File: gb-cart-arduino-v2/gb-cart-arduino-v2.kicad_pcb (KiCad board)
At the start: 2 copper layers, 57.5 x 53.5 mm, 18 parts, among them J1 Conn_01x16_Pin, U1 74HC595, U2 74HC595

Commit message: Rewired v2
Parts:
- removed Ce1: 10uF, Capacitor_SMD:C_1206_3216Metric
- removed Ra1, Ra2, Ra4: 470, Resistor_SMD:R_1206_3216Metric
- removed Rd8: 1k, Resistor_SMD:R_1206_3216Metric
- added C1: 10uF, Capacitor_SMD:C_1206_3216Metric, F.Cu at (150.5, 96.0)
- added Rd0: 1k, Resistor_SMD:R_1206_3216Metric, F.Cu at (114.5, 108.5)
- added Rl1: 470, Resistor_SMD:R_1206_3216Metric, F.Cu at (150.5, 108.0)
- added Rr1: 470, Resistor_SMD:R_1206_3216Metric, F.Cu at (150.5, 104.0)
- added Rw1: 470, Resistor_SMD:R_1206_3216Metric, F.Cu at (150.5, 100.0)
- moved Rd4 12.1 mm to (109.5, 96.5), turned to 0 degrees
- moved Rd5 11.3 mm to (109.5, 100.5)
- moved Rd3 11.1 mm to (114.5, 96.5)
- moved Rd7 9.97 mm to (109.5, 108.5)
- moved Rd1 8.23 mm to (114.5, 104.5)
- moved Rd6 8.06 mm to (109.5, 104.5)
- moved Rd2 6.84 mm to (114.5, 100.5)
- moved D1 6.50 mm to (150.6, 112.0), turned to 0 degrees
- moved Rreset1 5.63 mm to (102.5, 97.5), turned to 90 degrees
- moved J1 3.53 mm to (144.8, 119.5)
- moved U1 3.20 mm to (140.0, 101.5)
- moved U2 2.50 mm to (126.5, 101.5)
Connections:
- D1 pad 2: /VCC -> /LED
- J1 pad 7: /Address_Clock -> /Address_Latch
- J1 pad 8: /Address_Latch -> /Address_Clock
- Rd1 pad 1: /Data_7 -> /Data_1
- Rd2 pad 1: /Data_6 -> /Data_2
- Rd3 pad 1: /Data_5 -> /Data_3
- Rd5 pad 1: /Data_3 -> /Data_5
- Rd6 pad 1: /Data_2 -> /Data_6
- Rd7 pad 1: /Data_1 -> /Data_7
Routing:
- net /VCC: track 95.8 -> 130.5 mm, vias 8 -> 5
- net /GND: track 199.4 -> 173.0 mm, vias 7 -> 5
- net /Address_Clock: track 27.2 -> 43.4 mm, vias 2 -> 0
- net /Address_Latch: track 33.3 -> 43.7 mm, vias 2 -> 0
- net /Write: track 28.0 -> 37.6 mm
- net /Data_3: track 29.4 -> 35.2 mm
- net /Address_7: track 23.7 -> 18.2 mm
- net /Clock: track 41.7 -> 36.3 mm
- net /Address_0: track 15.2 -> 10.0 mm
- net /Address_6: track 21.4 -> 16.3 mm
- net /Address_5: track 19.4 -> 14.4 mm
- net /Data_2: track 30.8 -> 35.3 mm
- net /Serial_Chain: track 28.7 -> 24.4 mm
- net /Address_15: track 21.8 -> 17.5 mm
- net /LED: track 0.00 -> 4.02 mm
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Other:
- board size 57.5 x 53.5 mm -> 57.5 x 55 mm

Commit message: Update
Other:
- board size 57.5 x 55 mm -> 58.5 x 56.2 mm
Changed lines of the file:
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@@
 		(tags "resistor")
 		(property "Reference" "Rl1"
-			(at 0 -1.83 0)
+			(at 0 2 0)
 			(layer "F.SilkS")
 			(effects
@@
 		(tags "LED")
 		(property "Reference" "D1"
-			(at 0 -1.83 0)
+			(at -0.1 -2 0)
 			(layer "F.SilkS")
 			(effects
@@
 		)
 	)
-	(gr_rect
-		(start 97 66.5)
-		(end 154.5 121.5)
+	(gr_line
+		(start 97.5 66)
+		(end 154 66)
+		(stroke
+			(width 0.1)
+			(type default)
+		)
+		(layer "Edge.Cuts")
+	)
+	(gr_line
+		(start 96.5 121.175)
+		(end 96.5 67)
+		(stroke
+			(width 0.1)
+			(type default)
+		)
+		(layer "Edge.Cuts")
+	)
+	(gr_line
+		(start 154 122.175)
+		(end 97.5 122.175)
+		(stroke
+			(width 0.1)
+			(type default)
+		)
+		(layer "Edge.Cuts")
+	)
+	(gr_arc
+		(start 155 121.175)
+		(mid 154.707107 121.882107)
+		(end 154 122.175)
+		(stroke
+			(width 0.1)
+			(type default)
+		)
+		(layer "Edge.Cuts")
+	)
+	(gr_arc
+		(start 97.5 122.175)
+		(mid 96.792893 121.882107)
+		(end 96.5 121.175)
+		(stroke
+			(width 0.1)
+			(type default)
+		)
+		(layer "Edge.Cuts")
+	)
+	(gr_line
+		(start 155 67)
+		(end 155 121.175)
+		(stroke
+			(width 0.1)
+			(type default)
+		)
+		(layer "Edge.Cuts")
+	)
+	(gr_arc
+		(start 154 66)
+		(mid 154.707107 66.292893)
+		(end 155 67)
+		(stroke
+			(width 0.1)
+			(type default)
+		)
+		(layer "Edge.Cuts")
+	)
+	(gr_arc
+		(start 96.5 67)
+		(mid 96.792893 66.292893)
+		(end 97.5 66)
 		(stroke
 			(width 0.1)
 			(type default)
 		)
-		(fill no)
 		(layer "Edge.Cuts")
 	)
@@
 	)
 	(segment
-		(start 118.0385 95.001)
-		(end 118.0375 95)
-		(width 0.3)
-		(layer "F.Cu")
-		(net 7)
-	)
-	(segment
 		(start 116.314979 117.0235)
 		(end 115.0865 115.795021)
@@
 	)
 	(segment
-		(start 121.4775 116.5225)
-		(end 121.455 116.5)
-		(width 0.3)
-		(layer "F.Cu")
-		(net 10)
-	)
-	(segment
 		(start 115.5875 108.9125)
 		(end 116 108.5)
@@
 		(width 0.3)
 		(layer "F.Cu")
-		(net 22)
-	)
-	(segment
-		(start 133.501 95.001)
-		(end 133.502 95)
-		(width 0.3)
-		(layer "F.Cu")

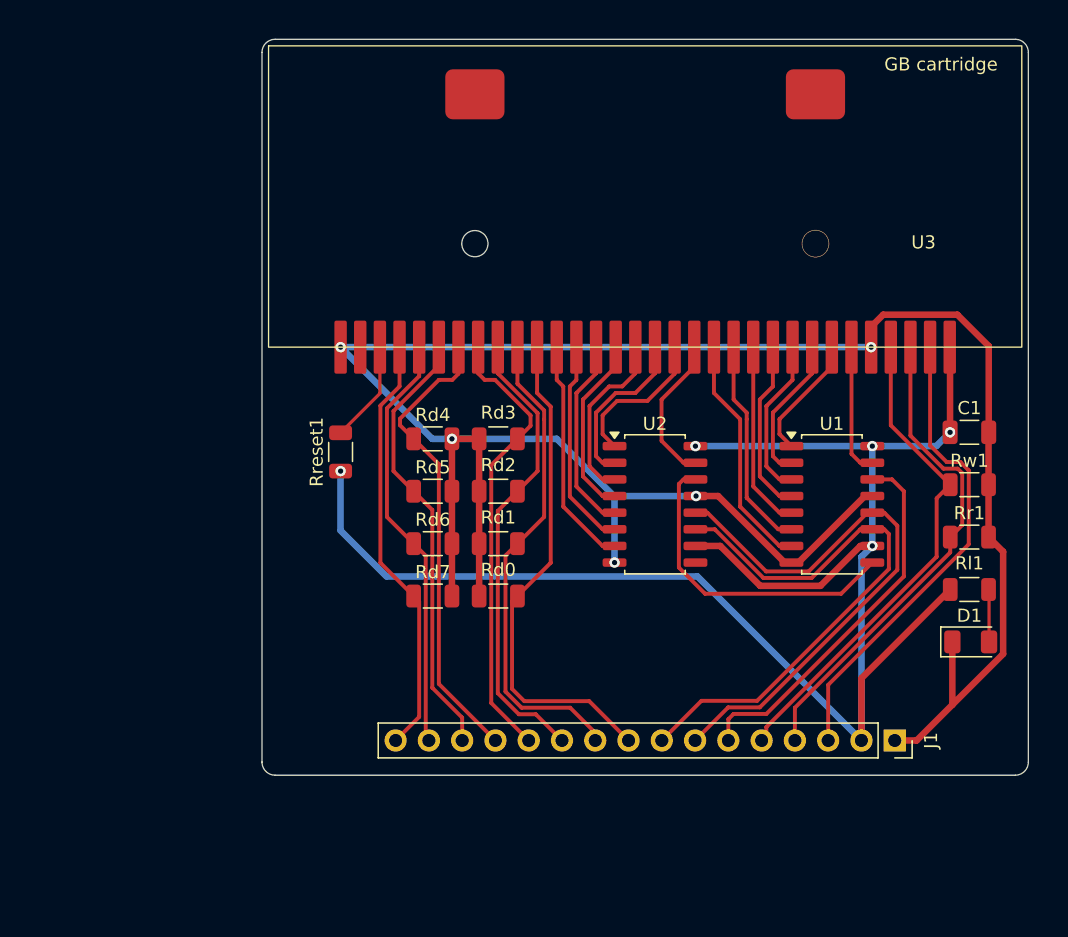
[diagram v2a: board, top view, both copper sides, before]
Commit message: Added texts
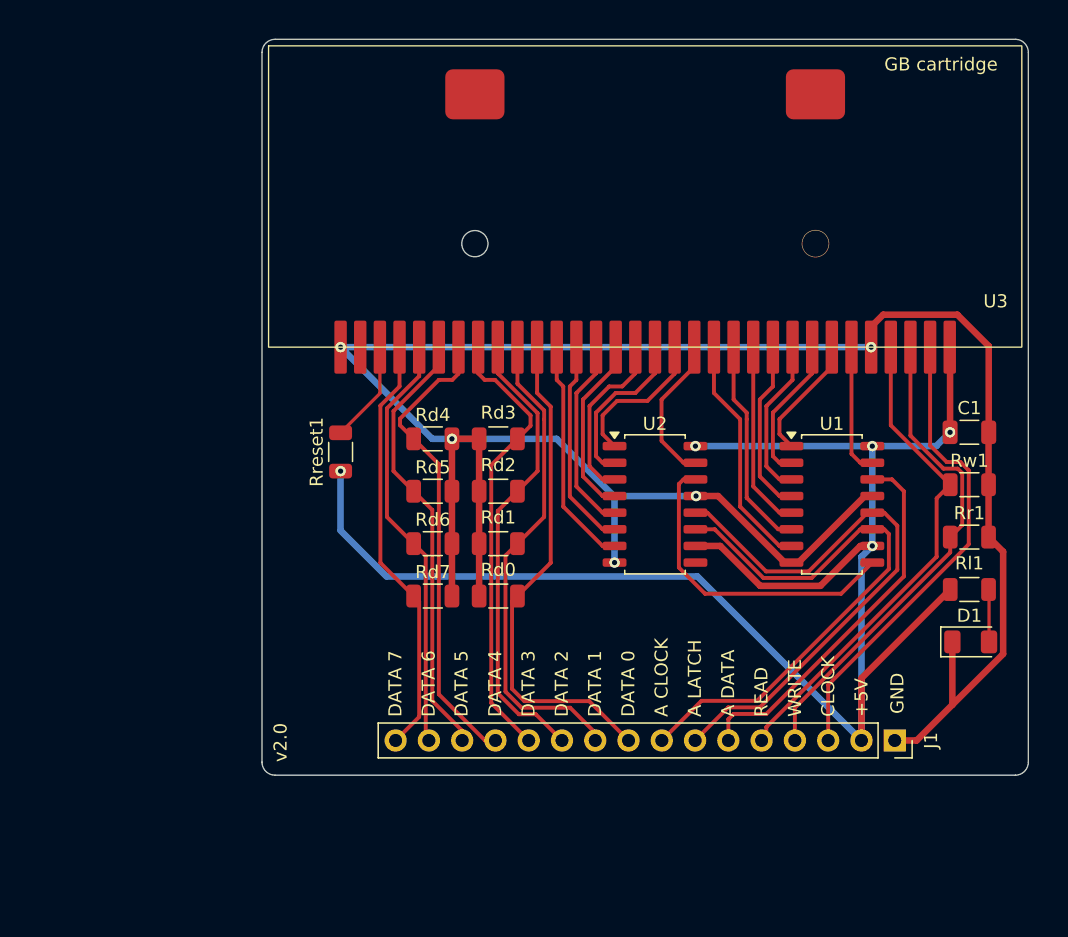
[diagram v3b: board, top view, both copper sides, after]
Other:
- board text added: "+5V"
- board text added: "A CLOCK"
- board text added: "A DATA"
- board text added: "A LATCH"
- board text added: "CLOCK"
- board text added: "DATA 0"
- board text added: "DATA 1"
- board text added: "DATA 2"
- board text added: "DATA 3"
- board text added: "DATA 4"
- board text added: "DATA 5"
- board text added: "DATA 6"
- board text added: "DATA 7"
- board text added: "GND"
- board text added: "READ"
- board text added: "WRITE"
- board text added: "https://github.com/GreenOlvi/gb-cart-reader-schematics"
- board text added: "v2.0"
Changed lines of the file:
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@@
 		(at 149 89.5)
 		(property "Reference" "U3"
-			(at -2 -8 0)
+			(at 3.5 -3.5 0)
 			(unlocked yes)
 			(layer "F.SilkS")
@@
 		(layer "Edge.Cuts")
 	)
+	(gr_text "CLOCK"
+		(at 139.72 117.725 90)
+		(layer "F.SilkS")
+		(effects
+			(font
+				(size 1 1)
+				(thickness 0.15)
+			)
+			(justify left)
+		)
+	)
+	(gr_text "A DATA"
+		(at 132.08 117.729 90)
+		(layer "F.SilkS")
+		(effects
+			(font
+				(size 1 1)
+				(thickness 0.15)
+			)
+			(justify left)
+		)
+	)
+	(gr_text "DATA 3"
+		(at 116.84 117.729 90)
+		(layer "F.SilkS")
+		(effects
+			(font
+				(size 1 1)
+				(thickness 0.15)
+			)
+			(justify left)
+		)
+	)
+	(gr_text "DATA 7"
+		(at 106.68 117.729 90)
+		(layer "F.SilkS")
+		(effects
+			(font
+				(size 1 1)
+				(thickness 0.15)
+			)
+			(justify left)
+		)
+	)
+	(gr_text "DATA 6"
+		(at 109.22 117.729 90)
+		(layer "F.SilkS")
+		(effects
+			(font
+				(size 1 1)
+				(thickness 0.15)
+			)
+			(justify left)
+		)
+	)
+	(gr_text "v2.0"
+		(at 98.5 121.175 90)
+		(layer "F.SilkS")
+		(effects
+			(font
+				(size 1 1)
+				(thickness 0.15)
+			)
+			(justify left bottom)
+		)
+	)
+	(gr_text "A CLOCK"
+		(at 127 117.729 90)
+		(layer "F.SilkS")
+		(effects
+			(font
+				(size 1 1)
+				(thickness 0.15)
+			)
+			(justify left)
+		)
+	)
+	(gr_text "GND"
+		(at 145 117.5 90)
+		(layer "F.SilkS")
+		(effects
+			(font
+				(size 1 1)
+				(thickness 0.15)
+			)
+			(justify left)
+		)
+	)
+	(gr_text "DATA 5"
+		(at 111.725 117.725 90)
+		(layer "F.SilkS")
+		(effects
+			(font
+				(size 1 1)
+				(thickness 0.15)
+			)
+			(justify left)
+		)
+	)
+	(gr_text "DATA 2"
+		(at 119.38 117.729 90)
+		(layer "F.SilkS")
+		(effects
+			(font
+				(size 1 1)
+				(thickness 0.15)
+			)
+			(justify left)
+		)
+	)
+	(gr_text "DATA 4"
+		(at 114.3 117.729 90)
+		(layer "F.SilkS")
+		(effects
+			(font
+				(size 1 1)
+				(thickness 0.15)
+			)
+			(justify left)
+		)
+	)
+	(gr_text "READ"
+		(at 134.62 117.725 90)
+		(layer "F.SilkS")
+		(effects
+			(font
+				(size 1 1)
+				(thickness 0.15)
+			)
+			(justify left)
+		)
+	)
+	(gr_text "DATA 0"
+		(at 124.46 117.725 90)
+		(layer "F.SilkS")
+		(effects
+			(font
+				(size 1 1)
+				(thickness 0.15)
+			)
+			(justify left)
+		)
+	)
+	(gr_text "WRITE"
+		(at 137.18 117.725 90)
+		(layer "F.SilkS")
+		(effects
+			(font
+				(size 1 1)
+				(thickness 0.15)
+			)
+			(justify left)
+		)
+	)
+	(gr_text "DATA 1"
+		(at 121.92 117.729 90)
+		(layer "F.SilkS")
+		(effects
+			(font
+				(size 1 1)
+				(thickness 0.15)
+			)
+			(justify left)
+		)
+	)
+	(gr_text "A LATCH"
+		(at 129.54 117.729 90)
+		(layer "F.SilkS")
+		(effects
+			(font
+				(size 1 1)
+				(thickness 0.15)
+			)
+			(justify left)
+		)
+	)
+	(gr_text "+5V"
+		(at 142.26 117.725 90)
+		(layer "F.SilkS")
+		(effects
+			(font
+				(size 1 1)
+				(thickness 0.15)
+			)
+			(justify left)
+		)
+	)
+	(gr_text "https://github.com/GreenOlvi/gb-cart-reader-schematics"
+		(at 154 68.5 0)
+		(layer "B.SilkS")
+		(effects
+			(font
+				(size 1.1 1.1)
+				(thickness 0.22)
+				(bold yes)
+			)
+			(justify left bottom mirror)
+		)
+	)
 	(segment
 		(start 113.075 108.5)
@@
 	)
 	(segment
-		(start 109.5 101.925)
-		(end 108.075 100.5)
+		(start 111.78 119.525)
+		(end 111.78 118.78)
 		(width 0.3)
 		(layer "F.Cu")
@@
 	)
 	(segment
-		(start 111.78 117.78)
-		(end 109.5 115.5)
+		(start 108.075 100.5)
+		(end 106.5375 98.9625)
 		(width 0.3)
 		(layer "F.Cu")
@@
 	)
 	(segment
-		(start 108.075 100.5)
-		(end 106.5375 98.9625)
+		(start 111.78 118.78)
+		(end 109.5 116.5)
 		(width 0.3)
 		(layer "F.Cu")
@@
 	)
 	(segment
-		(start 111.78 119.525)
-		(end 111.78 117.78)
+		(start 109.5 116.5)
+		(end 109.5 101.925)
 		(width 0.3)
 		(layer "F.Cu")
@@
 	)
 	(segment
-		(start 109.5 115.5)
-		(end 109.5 101.925)
+		(start 109.5 101.925)
+		(end 108.075 100.5)
 		(width 0.3)
 		(layer "F.Cu")
@@
 	)
 	(segment
-		(start 107.0385 95.4635)
+		(start 110 98.425)
 		(end 108.075 96.5)
 		(width 0.3)
@@
 	)
 	(segment
-		(start 110 98.425)
-		(end 108.075 96.5)
+		(start 113.525 119.525)
+		(end 110 116)
 		(width 0.3)
 		(layer "F.Cu")
@@
 	)
 	(segment
-		(start 110 115.205)
-		(end 110 98.425)
+		(start 107.0385 95.4635)
+		(end 108.075 96.5)
 		(width 0.3)
 		(layer "F.Cu")
@@
 	)
 	(segment
+		(start 111.5 91.525)
+		(end 111.025 92)
+		(width 0.3)
+		(layer "F.Cu")
+		(net 15)
+	)
+	(segment
 		(start 114.32 119.525)
-		(end 110 115.205)
+		(end 113.525 119.525)
 		(width 0.3)
 		(layer "F.Cu")
@@
 	)
 	(segment
-		(start 111.5 91.525)
-		(end 111.025 92)
+		(start 110 116)
+		(end 110 98.425)
 		(width 0.3)
 		(layer "F.Cu")

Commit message: Final sent to production
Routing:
- net /GND: track 173.0 -> 176.2 mm, vias 5 -> 4
- added copper zone on B.Cu, net /GND
- added copper zone on F.Cu, net /GND
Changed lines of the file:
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@@
 			(outputformat 1)
 			(mirror no)
-			(drillshape 1)
+			(drillshape 0)
 			(scaleselection 1)
-			(outputdirectory "")
+			(outputdirectory "gerber/")
 		)
 	)
@@
 		)
 	)
-	(gr_text "v2.0"
-		(at 98.5 121.175 90)
-		(layer "F.SilkS")
-		(effects
-			(font
-				(size 1 1)
-				(thickness 0.15)
-			)
-			(justify left bottom)
-		)
-	)
 	(gr_text "A CLOCK"
 		(at 127 117.729 90)
@@
 		)
 	)
+	(gr_text "v2.0"
+		(at 154 70.5 0)
+		(layer "B.SilkS")
+		(effects
+			(font
+				(size 1 1)
+				(thickness 0.15)
+			)
+			(justify left bottom mirror)
+		)
+	)
 	(gr_text "https://github.com/GreenOlvi/gb-cart-reader-schematics"
 		(at 154 68.5 0)
@@
 	)
 	(segment
+		(start 102.5 87.475)
+		(end 102.5 89.5)
+		(width 0.5)
+		(layer "F.Cu")
+		(net 2)
+	)
+	(segment
 		(start 111 104.5)
 		(end 111 108.5)
@@
 	)
 	(segment
+		(start 144 87.024)
+		(end 143.917714 87.024)
+		(width 0.5)
+		(layer "F.Cu")
+		(net 2)
+	)
+	(segment
 		(start 143.917714 87.024)
 		(end 143 87.941714)
@@
 	(segment
 		(start 149.582286 87.024)
-		(end 143.917714 87.024)
+		(end 144 87.024)
 		(width 0.5)
 		(layer "F.Cu")
@@
 	)
 	(segment
+		(start 102.951 87.024)
+		(end 102.5 87.475)
+		(width 0.5)
+		(layer "F.Cu")
+		(net 2)
+	)
+	(segment
 		(start 151.9625 104)
 		(end 151.9625 96.0125)
@@
 	)
 	(segment
+		(start 144 87.024)
+		(end 102.951 87.024)
+		(width 0.5)
+		(layer "F.Cu")
+		(net 2)
+	)
+	(segment
 		(start 129.635 100.865)
 		(end 131.319878 100.865)
@@
 	)
 	(via
-		(at 143 89.5)
-		(size 0.8)
-		(drill 0.4)
-		(layers "F.Cu" "B.Cu")
-		(net 2)
-	)
-	(via
 		(at 102.5 89.5)
 		(size 0.8)
@@
 	)
 	(segment
-		(start 143 89.5)
-		(end 102.5 89.5)
-		(width 0.5)
-		(layer "B.Cu")
-		(net 2)
-	)
-	(segment
 		(start 123.4125 101.0875)
 		(end 123.4125 105.945)
@@
 		(net 37)
 	)
+	(zone
+		(net 2)
+		(net_name "/GND")
+		(layers "F.Cu" "B.Cu")
+		(hatch edge 0.5)
+		(connect_pads
+			(clearance 0.5)
+		)
+		(min_thickness 0.25)
+		(filled_areas_thickness no)
+		(fill yes
+			(thermal_gap 0.5)
+			(thermal_bridge_width 0.5)
+		)
+		(polygon
+			(pts
+				(xy 95 65) (xy 156 65) (xy 156 123.5) (xy 95 123.5)
+			)
+		)
+	)
 	(embedded_fonts no)

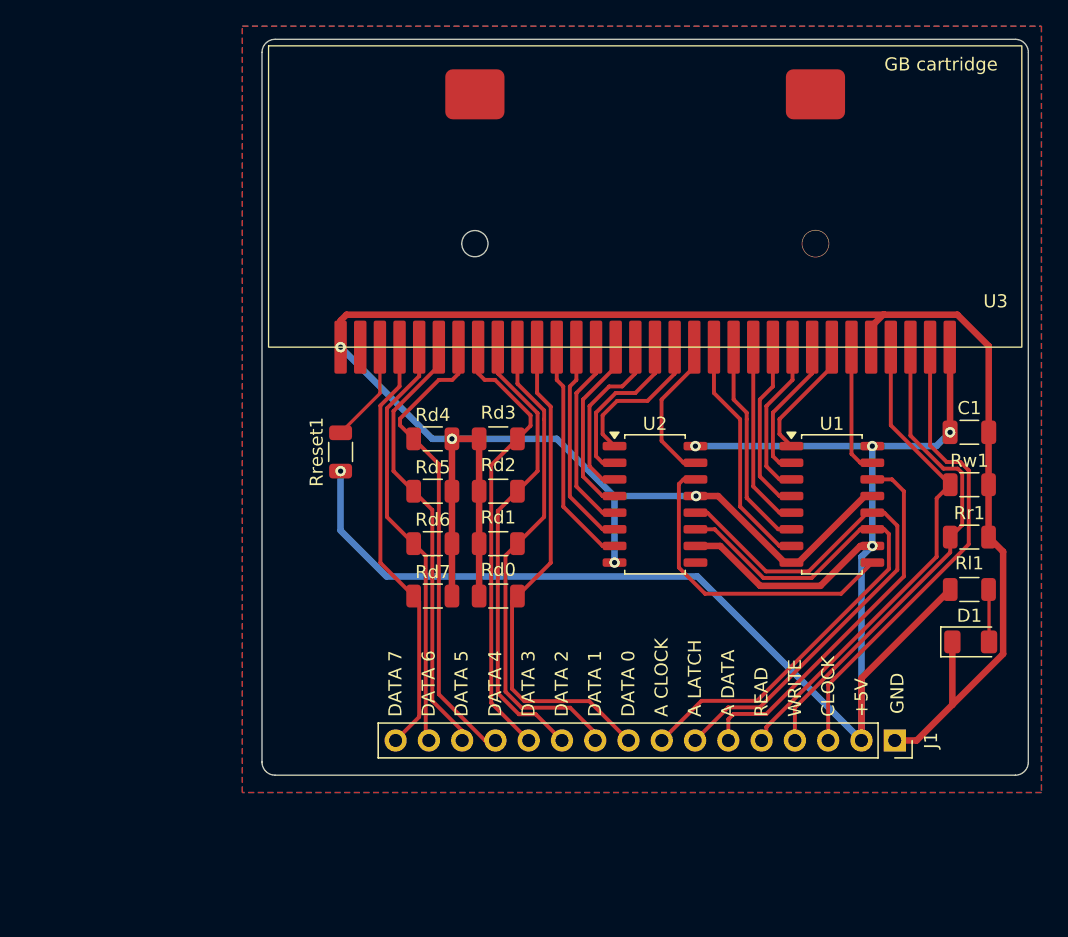
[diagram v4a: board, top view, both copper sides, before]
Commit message: Reversed gb cart connector footprint
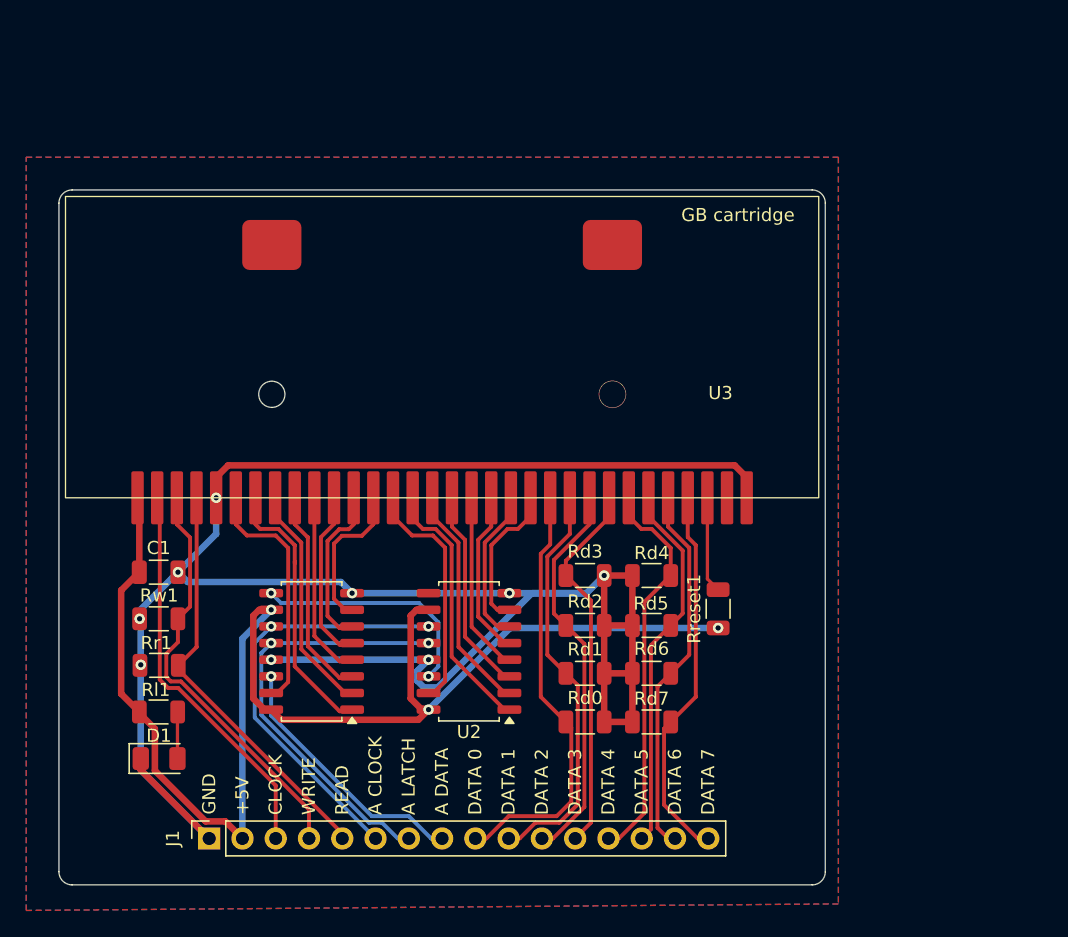
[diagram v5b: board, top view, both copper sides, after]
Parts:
- moved C1 62.8 mm to (88.6, 106.7)
- moved Rw1 62.7 mm to (88.6, 110.2), turned to 180 degrees
- moved Rr1 62.6 mm to (88.6, 113.8), turned to 180 degrees
- moved Rl1 62.6 mm to (88.6, 117.3)
- moved D1 62.6 mm to (88.6, 120.9)
- moved J1 52.9 mm to (92.5, 127.0), turned to 90 degrees
- moved U1 41.3 mm to (100.3, 112.7), turned to 180 degrees
- moved Rreset1 31.2 mm to (131.3, 109.5)
- moved Rd4 19.7 mm to (126.2, 106.9), turned to 180 degrees
- moved Rd5 19.6 mm to (126.2, 110.7), turned to 180 degrees
- moved Rd6 19.4 mm to (126.2, 114.4), turned to 180 degrees
- moved U3 19.3 mm to (133.5, 101.0)
- moved Rd7 19.3 mm to (126.2, 118.1), turned to 180 degrees
- moved U2 18.1 mm to (112.3, 112.7), turned to 180 degrees
- moved Rd3 12.4 mm to (121.2, 106.9), turned to 0 degrees
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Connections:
- J1 pad 6: /Address_Data -> /Address_Clock
- J1 pad 8: /Address_Clock -> /Address_Data
- Rr1 pad 1: /Write -> /Read
- Rw1 pad 1: /Read -> /Write
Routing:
- net /VCC: track 130.5 -> 106.2 mm, vias 5 -> 3
- net /Address_1: track 9.59 -> 20.8 mm
- net /Address_Clock: track 43.4 -> 32.5 mm, vias 0 -> 2
- net /Address_Latch: track 43.7 -> 33.0 mm, vias 0 -> 2
- net /Address_Data: track 28.8 -> 19.9 mm, vias 0 -> 1
- net /Address_0: track 10.0 -> 18.7 mm
- net /Address_9: track 11.6 -> 20.0 mm
- net /Address_8: track 11.5 -> 18.2 mm
- net /Data_3: track 35.2 -> 28.7 mm
- net /Address_2: track 11.2 -> 17.7 mm
- net /Serial_Chain: track 24.4 -> 18.1 mm, vias 0 -> 2
- net /Address_15: track 17.5 -> 11.4 mm
- net /Clock: track 36.3 -> 30.2 mm
- net /Read: track 37.9 -> 31.9 mm
- net /Data_4: track 36.0 -> 30.2 mm
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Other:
- board size 58.5 x 56.2 mm -> 58.5 x 53 mm
- board text removed: "https://github.com/GreenOlvi/gb-cart-reader-schematics"
- board text removed: "v2.0"
